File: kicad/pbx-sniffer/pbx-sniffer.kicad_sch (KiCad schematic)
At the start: 1 part

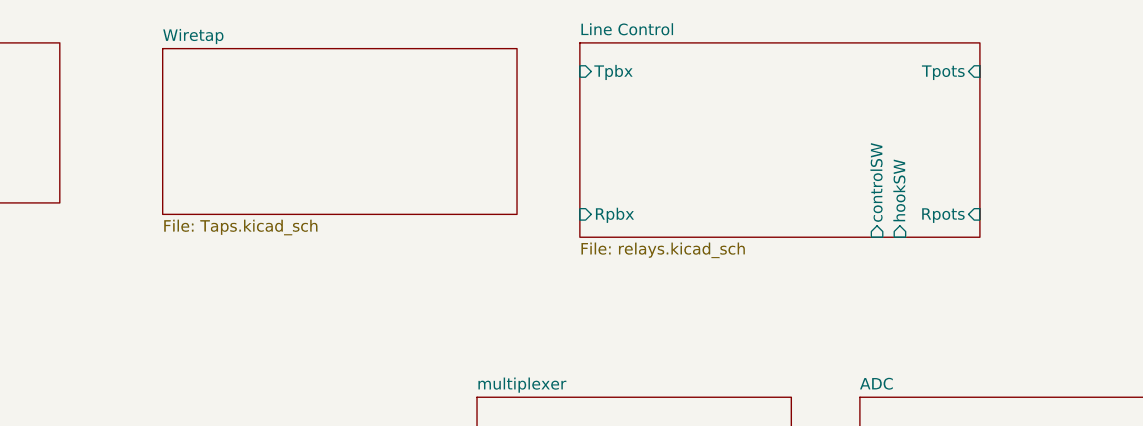
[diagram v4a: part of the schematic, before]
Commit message: working on duplicating adc and control circuits between phone jacks
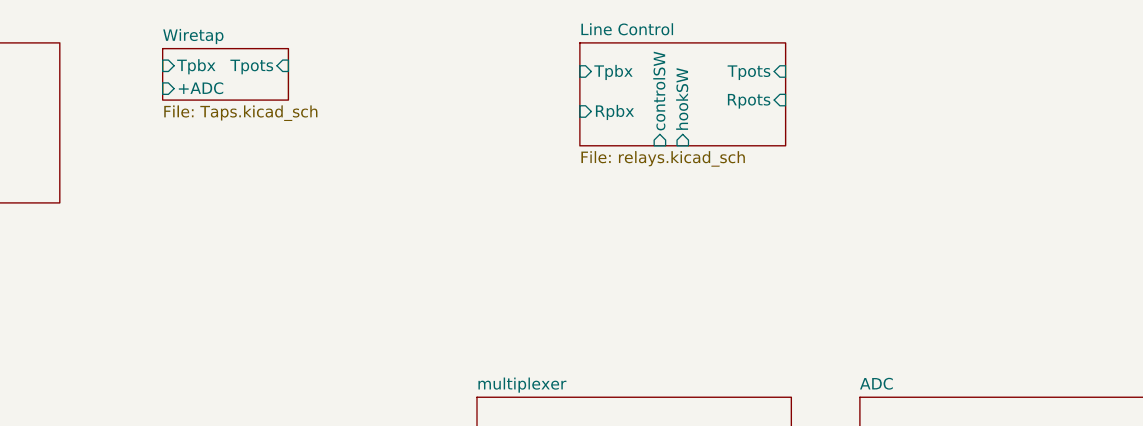
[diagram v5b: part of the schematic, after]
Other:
- sheet Wiretap ports: added +ADC, Tpbx, Tpots; removed none
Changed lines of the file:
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@@
 	(sheet
 		(at 161.29 15.875)
-		(size 39.37 18.415)
+		(size 13.97 5.715)
 		(exclude_from_sim no)
 		(in_bom yes)
@@
 		)
 		(property "Sheetfile" "Taps.kicad_sch"
-			(at 161.29 34.8746 0)
-			(effects
-				(font
-					(size 1.27 1.27)
-				)
-				(justify left top)
+			(at 161.29 22.1746 0)
+			(effects
+				(font
+					(size 1.27 1.27)
+				)
+				(justify left top)
+			)
+		)
+		(pin "+ADC" input
+			(at 161.29 20.32 180)
+			(effects
+				(font
+					(size 1.27 1.27)
+				)
+				(justify left)
+			)
+		)
+		(pin "Tpbx" input
+			(at 161.29 17.78 180)
+			(effects
+				(font
+					(size 1.27 1.27)
+				)
+				(justify left)
+			)
+		)
+		(pin "Tpots" input
+			(at 175.26 17.78 0)
+			(effects
+				(font
+					(size 1.27 1.27)
+				)
+				(justify right)
 			)
 		)
@@
 	(sheet
 		(at 207.645 15.24)
-		(size 44.45 21.59)
+		(size 22.86 11.43)
 		(exclude_from_sim no)
 		(in_bom yes)
@@
 		)
 		(property "Sheetfile" "relays.kicad_sch"
-			(at 207.645 37.4146 0)
+			(at 207.645 27.2546 0)
 			(effects
 				(font
@@
 		)
 		(pin "controlSW" input
-			(at 240.665 36.83 270)
+			(at 216.535 26.67 270)
 			(effects
 				(font
@@
 		)
 		(pin "hookSW" input
-			(at 243.205 36.83 270)
+			(at 219.075 26.67 270)
 			(effects
 				(font
@@
 		)
 		(pin "Rpbx" input
-			(at 207.645 34.29 180)
+			(at 207.645 22.86 180)
 			(effects
 				(font
@@
 		)
 		(pin "Rpots" input
-			(at 252.095 34.29 0)
+			(at 230.505 21.59 0)
 			(effects
 				(font
@@
 		)
 		(pin "Tpots" input
-			(at 252.095 18.415 0)
-			(effects
-				(font
+			(at 230.505 18.415 0)
+			(effects
+				(font

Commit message: finished jack hierachial labels. started putting them on the main sch
(pts
        (xy 45.72 86.36) (xy 59.69 86.36)
    )
    (stroke (width 0) (type default))
    (uuid "8ace12cb-ee30-47b7-8bb3-4f75477c25bd")
)
(wire
    (pts
        (xy 45.72 7.62) (xy 59.69 7.62)
    )
    (stroke (width 0) (type default))
    (uuid "84b70951-4dad-4be3-9586-537893c9e04a")
)
(wire
    (pts
        (xy 45.72 25.4) (xy 59.69 25.4)
    )
    (stroke (width 0) (type default))
    (uuid "a596782f-ae99-45f2-bc6f-3ff7a57a1ee7")
)
(wire
    (pts
        (xy 45.72 22.86) (xy 59.69 22.86)
    )
    (stroke (width 0) (type default))
    (uuid "eaa8a2fd-b211-43aa-899e-a54c76015a70")
)
(wire
    (pts
        (xy 45.72 43.18) (xy 59.69 43.18)
    )
    (stroke (width 0) (type default))
    (uuid "fbbaa87e-b2d5-48b8-b043-e998d4ad25a1")
)
(wire
    (pts
        (xy 45.72 81.28) (xy 59.69 81.28)
    )
    (stroke (width 0) (type default))
    (uuid "74339180-59e3-4aa4-9224-65ca846e8e3c")
)
(wire
    (pts
        (xy 45.72 55.88) (xy 59.69 55.88)
    )
    (stroke (width 0) (type default))
    (uuid "f75722ba-5479-4928-addf-4bcf03d2e5a1")
)
(wire
    (pts
        (xy 45.72 12.7) (xy 59.69 12.7)
    )
    (stroke (width 0) (type default))
    (uuid "b067b129-586d-4458-9293-a7c491fcfe84")
)
(wire
    (pts
        (xy 45.72 45.72) (xy 59.69 45.72)
    )
    (stroke (width 0) (type default))
    (uuid "89d7089e-feae-4ac4-80ce-7609117a820b")
)
(wire
    (pts
        (xy 45.72 27.94) (xy 59.69 27.94)
    )
    (stroke (width 0) (type default))
    (uuid "1f557dbd-c289-4d27-9dcc-8cd8b89deadf")
)
(wire
    (pts
        (xy 45.72 15.24) (xy 59.69 15.24)
    )
    (stroke (width 0) (type default))
    (uuid "be64a9fe-163d-449f-888e-4a585432744b")
)
(wire
    (pts
        (xy 45.72 48.26) (xy 59.69 48.26)
    )
    (stroke (width 0) (type default))
    (uuid "d4da723b-c601-47e4-9bb4-8c723ce5d480")
)
(wire
    (pts
        (xy 45.72 53.34) (xy 59.69 53.34)
    )
    (stroke (width 0) (type default))
    (uuid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
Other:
- sheet Input Phone Jacks ports: added Rpbx0, Rpbx1, Rpbx10, Rpbx11, Rpbx12, Rpbx13, Rpbx14, Rpbx15, Rpbx16, Rpbx17, Rpbx18, Rpbx19, Rpbx2, Rpbx20, Rpbx21, Rpbx22, Rpbx23, Rpbx3, Rpbx4, Rpbx5, Rpbx6, Rpbx7, Rpbx8, Rpbx9, Tpbx0, Tpbx1, Tpbx10, Tpbx11, Tpbx12, Tpbx13, Tpbx14, Tpbx15, Tpbx16, Tpbx17, Tpbx18, Tpbx19, Tpbx2, Tpbx20, Tpbx21, Tpbx22, Tpbx23, Tpbx3, Tpbx4, Tpbx5, Tpbx6, Tpbx7, Tpbx8, Tpbx9, controlSW0, controlSW1, controlSW10, controlSW11, controlSW12, controlSW13, controlSW14, controlSW15, controlSW16, controlSW17, controlSW18, controlSW19, controlSW2, controlSW20, controlSW21, controlSW22, controlSW23, controlSW3, controlSW4, controlSW5, controlSW6, controlSW7, controlSW8, controlSW9, hookSW0, hookSW1, hookSW10, hookSW11, hookSW12, hookSW13, hookSW14, hookSW15, hookSW16, hookSW17, hookSW18, hookSW19, hookSW2, hookSW20, hookSW21, hookSW22, hookSW23, hookSW3, hookSW4, hookSW5, hookSW6, hookSW7, hookSW8, hookSW9, ptRX0, ptRX1, ptRX10, ptRX11, ptRX12, ptRX13, ptRX14, ptRX15, ptRX16, ptRX17, ptRX18, ptRX19, ptRX2, ptRX20, ptRX21, ptRX22, ptRX23, ptRX3, ptRX4, ptRX5, ptRX6, ptRX7, ptRX8, ptRX9, ptTX0, ptTX1, ptTX10, ptTX11, ptTX12, ptTX13, ptTX14, ptTX15, ptTX16, ptTX17, ptTX18, ptTX19, ptTX2, ptTX20, ptTX21, ptTX22, ptTX23, ptTX3, ptTX4, ptTX5, ptTX6, ptTX7, ptTX8, ptTX9; removed none
- sheet Output Phone Jacks ports: added ADC0, ADC1, ADC10, ADC11, ADC12, ADC13, ADC14, ADC15, ADC16, ADC17, ADC18, ADC19, ADC2, ADC20, ADC21, ADC22, ADC23, ADC3, ADC4, ADC5, ADC6, ADC7, ADC8, ADC9, Rpbx0, Rpbx1, Rpbx10, Rpbx11, Rpbx12, Rpbx13, Rpbx14, Rpbx15, Rpbx16, Rpbx17, Rpbx18, Rpbx19, Rpbx2, Rpbx20, Rpbx21, Rpbx22, Rpbx23, Rpbx3, Rpbx4, Rpbx5, Rpbx6, Rpbx7, Rpbx8, Rpbx9, Tpbx0, Tpbx1, Tpbx10, Tpbx11, Tpbx12, Tpbx13, Tpbx14, Tpbx15, Tpbx16, Tpbx17, Tpbx18, Tpbx19, Tpbx2, Tpbx20, Tpbx21, Tpbx22, Tpbx23, Tpbx3, Tpbx4, Tpbx5, Tpbx6, Tpbx7, Tpbx8, Tpbx9, ptRX0, ptRX1, ptRX10, ptRX11, ptRX12, ptRX13, ptRX14, ptRX15, ptRX16, ptRX17, ptRX18, ptRX19, ptRX2, ptRX20, ptRX21, ptRX22, ptRX23, ptRX3, ptRX4, ptRX5, ptRX6, ptRX7, ptRX8, ptRX9, ptTX0, ptTX1, ptTX10, ptTX11, ptTX12, ptTX13, ptTX14, ptTX15, ptTX16, ptTX17, ptTX18, ptTX19, ptTX2, ptTX20, ptTX21, ptTX22, ptTX23, ptTX3, ptTX4, ptTX5, ptTX6, ptTX7, ptTX8, ptTX9; removed none
- moved on the sheet: U1A, U1B

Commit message: add new gnd pins to nucleo symbol
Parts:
- U1: footprint Connector_PinHeader_2.54mm:PinHeader_2x19_P2.54mm_Vertical -> Connector_PinSocket_2.54mm:PinSocket_2x19_P2.54mm_Vertical
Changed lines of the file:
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@@
 			)
 		)
-		(property "Footprint" "Connector_PinHeader_2.54mm:PinHeader_2x19_P2.54mm_Vertical"
+		(property "Footprint" "Connector_PinSocket_2.54mm:PinSocket_2x19_P2.54mm_Vertical"
 			(at 172.72 100.33 0)
 			(effects
@@
 			)
 		)
-		(property "Footprint" "Connector_PinHeader_2.54mm:PinHeader_2x19_P2.54mm_Vertical"
+		(property "Footprint" "Connector_PinSocket_2.54mm:PinSocket_2x19_P2.54mm_Vertical"
 			(at 139.7 109.22 0)
 			(effects

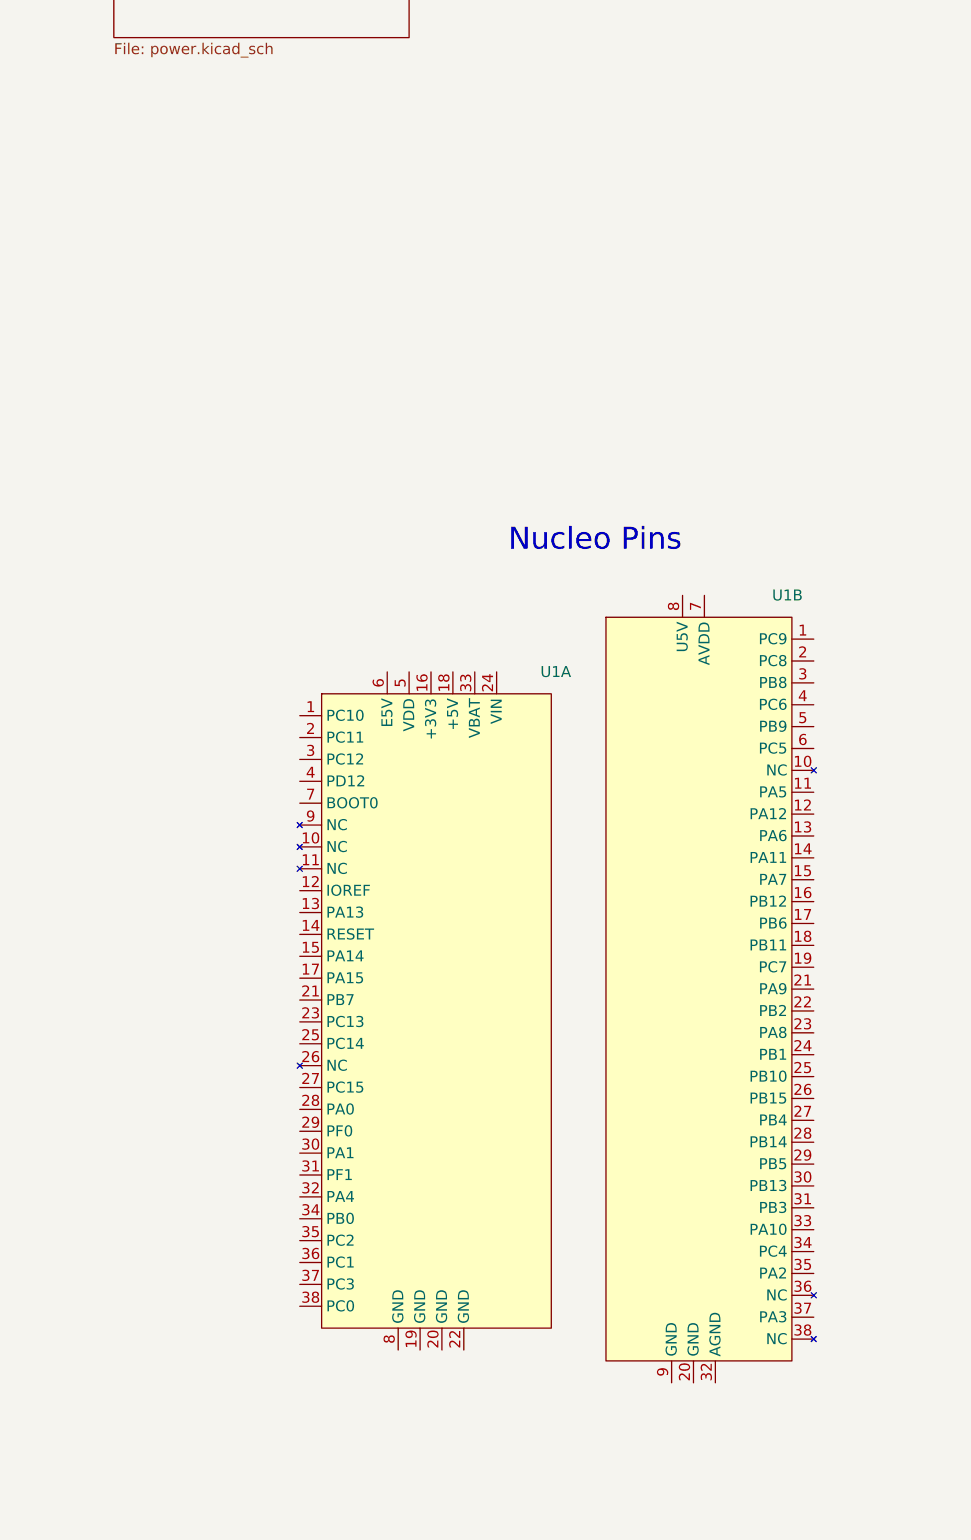
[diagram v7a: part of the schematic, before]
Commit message: add footprint for stm32
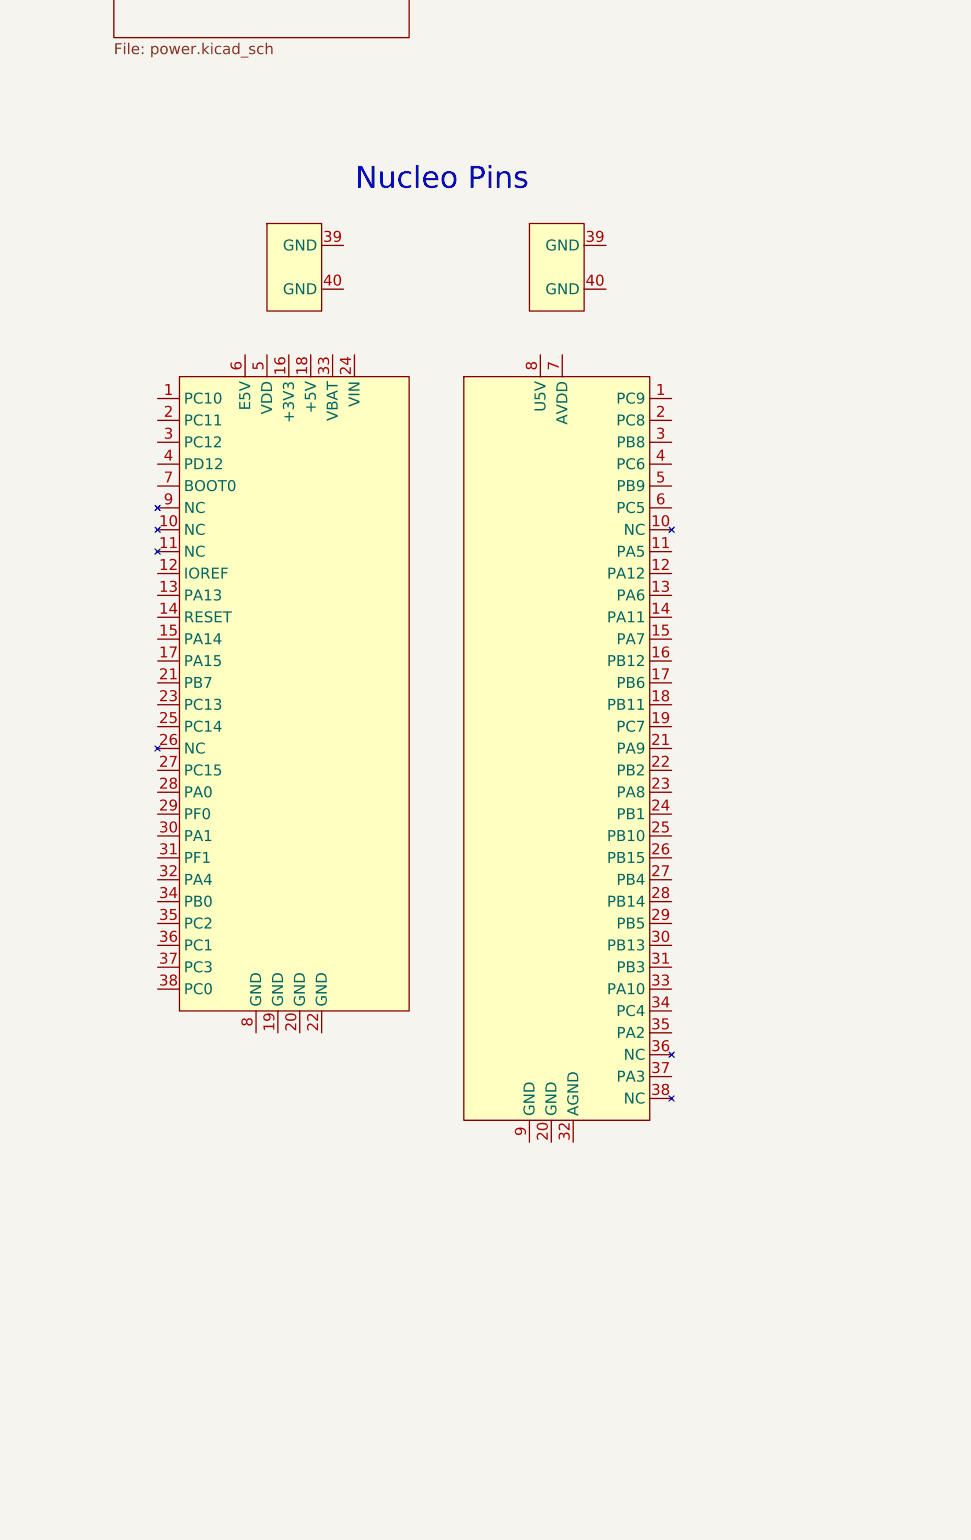
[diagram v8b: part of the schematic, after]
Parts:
- added unit 3 of U1
- added unit 4 of U1
- U1: footprint Connector_PinSocket_2.54mm:PinSocket_2x19_P2.54mm_Vertical -> Phones:STM32NucleoF303RE
